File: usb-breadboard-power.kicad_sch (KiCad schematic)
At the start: 48 parts, among them J1 USB_C_Receptacle_PowerOnly_6P, J2 Conn_02x02, J3 Conn_02x02, J4 Conn_01x03, Q3 DMP6110, SW1 SW_DIP_x03, U1 CYPD3177, U2 BD33FC0FP, U3 LM339

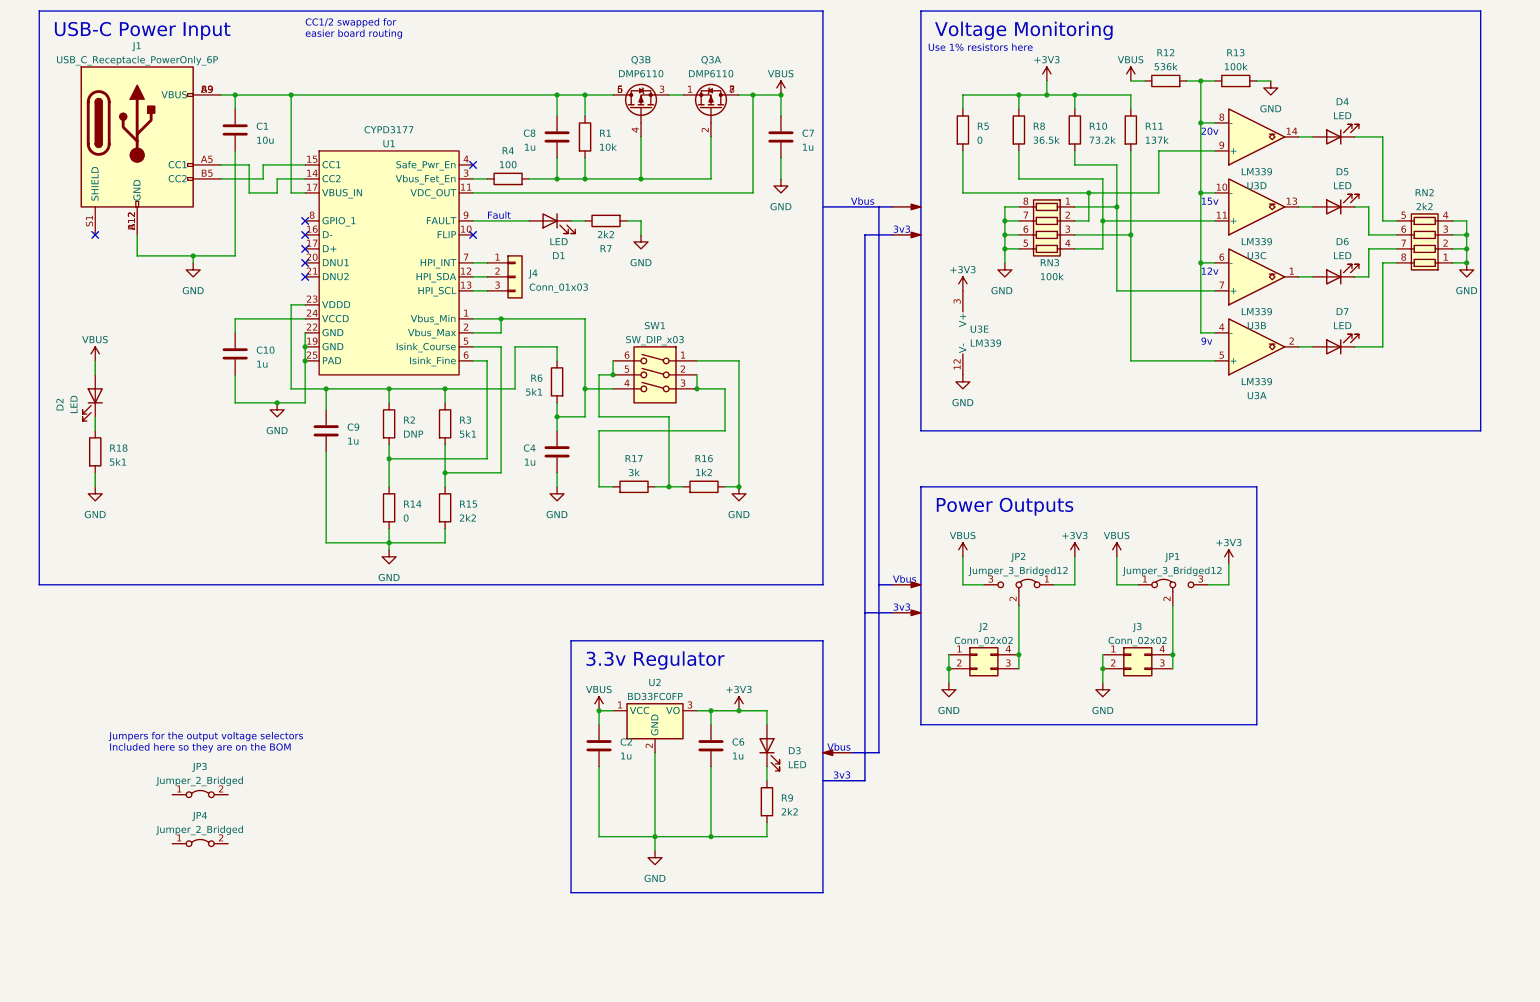
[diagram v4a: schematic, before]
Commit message: Updated gitignore and added fuse
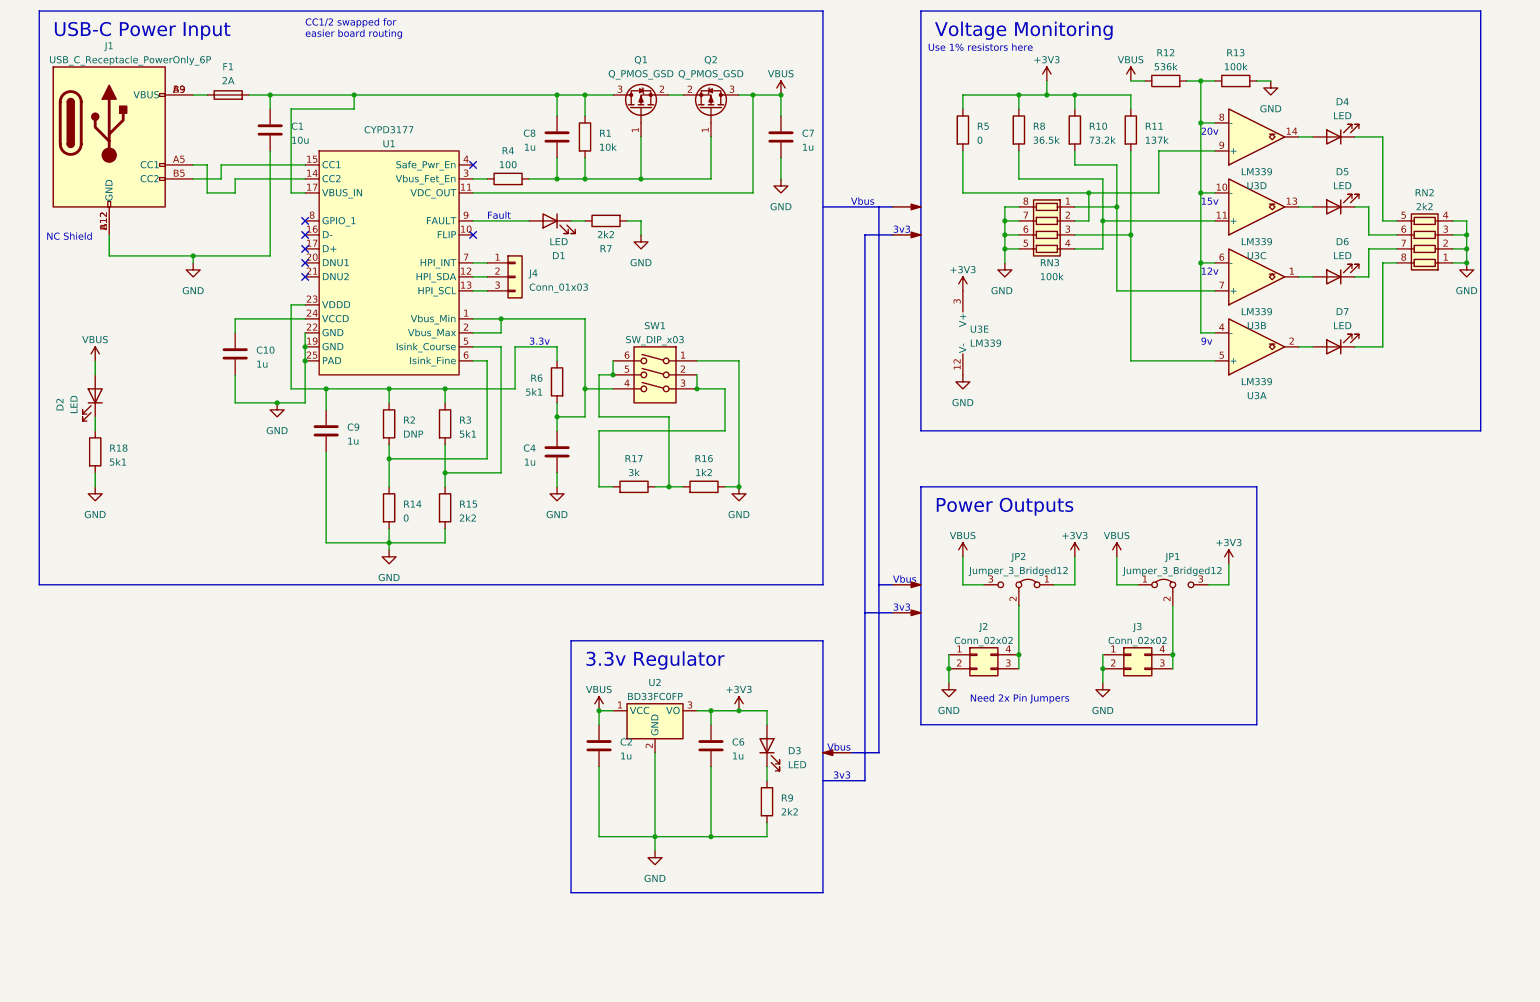
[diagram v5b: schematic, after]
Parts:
- removed JP3, JP4: Jumper_2_Bridged, symbol Jumper:Jumper_2_Bridged
- removed Q3: DMP6110, Package_SO:SO-8_5.3x6.2mm_P1.27mm, symbol Device:Q_Dual_PMOS_S1G1D2S2G2D1
- added F1: 2A, Fuse:Fuse_1812_4532Metric, symbol Device:Fuse
- added Q1, Q2: Q_PMOS_GSD, Package_TO_SOT_SMD:SOT-23-3, symbol Device:Q_PMOS_GSD
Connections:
- net VBUS: now also Q2.3 (D)
- net at U1.17 (VBUS_IN): now also C1.1, C8.1, R1.1, F1.2, Q1.3 (D)
- net at C8.2, R1.2, R4.2: now also Q1.1 (G), Q2.1 (G)
- new net: F1.1, J1.A9 (VBUS), J1.B9 (VBUS)
- new net: Q1.2 (S), Q2.2 (S)
- no-connect marks 8 -> 7
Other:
- note added: "3.3v"
- note added: "NC Shield"
- note added: "Need 2x Pin Jumpers"
- note removed: "Jumpers for the output voltage selectors Included here so they are on the BOM"
- moved on the sheet: C1

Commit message: More small fixes
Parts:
- R10: value 73.2k -> 90.9k; DPN-m 652-CR1206FX-7322ELF -> 652-CR1206FX-9092ELF; MPN-m CR1206-FX-7322ELF -> CR1206FX-9092ELF
- R11: value 137k -> 162k; DPN-m 652-CR1206FX-1373ELF -> 652-CR1206FX-1623ELF; MPN-m CR1206-FX-1373ELF -> CR1206FX-1623ELF
- R5: value 0 -> 10.5k; DPN-m 652-CR1206-J/-000ELF -> 652-CR1206FX-1052ELF; MPN-m CR1206-J/-000ELF -> CR1206FX-1052ELF
- R8: value 36.5k -> 49.9k; DPN-m 652-CR1206FX-3652ELF -> 652-CR1206FX-4992ELF; MPN-m CR1206-FX-3652ELF -> CR1206FX-4992ELF
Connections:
- net at U1.17 (VBUS_IN): now also C1.1, C8.1, F1.2, Q1.3 (D), R1.1
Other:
- note added: "3.3v internal"
- note added: "Check this is correct"
- note added: "Request 2A from the PSU"
- note removed: "3.3v"
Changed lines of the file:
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@@
     (effects (font (size 1.27 1.27)) (justify left bottom))
   )
-  (text "3.3v" (at 106.68 78.74 0)
+  (text "3.3v internal" (at 102.87 78.74 0)
     (effects (font (size 1.27 1.27)) (justify left bottom))
   )
@@
     (effects (font (size 1.27 1.27)) (justify left bottom))
   )
+  (text "Request 2A from\nthe PSU" (at 85.09 118.11 0)
+    (effects (font (size 1.27 1.27)) (justify left bottom))
+  )
   (text "Vbus" (at 165.1 53.34 0)
     (effects (font (size 1.27 1.27)) (justify left bottom))
@@
   )
   (text "Vbus" (at 172.72 121.92 0)
+    (effects (font (size 1.27 1.27)) (justify left bottom))
+  )
+  (text "Check this is correct" (at 107.95 57.15 0)
     (effects (font (size 1.27 1.27)) (justify left bottom))
   )
@@
       (effects (font (size 1.27 1.27)) (justify left))
     )
-    (property "Value" "73.2k" (at 208.28 41.275 0)
+    (property "Value" "90.9k" (at 208.28 41.275 0)
       (effects (font (size 1.27 1.27)) (justify left))
     )
@@
       (effects (font (size 1.27 1.27)) hide)
     )
-    (property "DPN-m" "652-CR1206FX-7322ELF" (at 205.74 39.37 0)
-      (effects (font (size 1.27 1.27)) hide)
-    )
-    (property "MPN-m" "CR1206-FX-7322ELF" (at 205.74 39.37 0)
+    (property "DPN-m" "652-CR1206FX-9092ELF" (at 205.74 39.37 0)
+      (effects (font (size 1.27 1.27)) hide)
+    )
+    (property "MPN-m" "CR1206FX-9092ELF" (at 205.74 39.37 0)
       (effects (font (size 1.27 1.27)) hide)
     )
@@
       (effects (font (size 1.27 1.27)) (justify left))
     )
-    (property "Value" "0" (at 187.96 41.275 0)
+    (property "Value" "10.5k" (at 187.96 41.275 0)
       (effects (font (size 1.27 1.27)) (justify left))
     )
@@
       (effects (font (size 1.27 1.27)) hide)
     )
-    (property "DPN-m" "652-CR1206-J/-000ELF " (at 185.42 39.37 0)
-      (effects (font (size 1.27 1.27)) hide)
-    )
-    (property "MPN-m" "CR1206-J/-000ELF " (at 185.42 39.37 0)
+    (property "DPN-m" "652-CR1206FX-1052ELF" (at 185.42 39.37 0)
+      (effects (font (size 1.27 1.27)) hide)
+    )
+    (property "MPN-m" "CR1206FX-1052ELF" (at 185.42 39.37 0)
       (effects (font (size 1.27 1.27)) hide)
     )
@@
       (effects (font (size 1.27 1.27)) (justify left))
     )
-    (property "Value" "137k" (at 218.44 41.275 0)
+    (property "Value" "162k" (at 218.44 41.275 0)
       (effects (font (size 1.27 1.27)) (justify left))
     )
@@
       (effects (font (size 1.27 1.27)) hide)
     )
-    (property "DPN-m" "652-CR1206FX-1373ELF" (at 215.9 39.37 0)
-      (effects (font (size 1.27 1.27)) hide)
-    )
-    (property "MPN-m" "CR1206-FX-1373ELF" (at 215.9 39.37 0)
+    (property "DPN-m" "652-CR1206FX-1623ELF" (at 215.9 39.37 0)
+      (effects (font (size 1.27 1.27)) hide)
+    )
+    (property "MPN-m" "CR1206FX-1623ELF" (at 215.9 39.37 0)
       (effects (font (size 1.27 1.27)) hide)
     )
@@
       (effects (font (size 1.27 1.27)) (justify left))
     )
-    (property "Value" "36.5k" (at 198.12 41.275 0)
+    (property "Value" "49.9k" (at 198.12 41.275 0)
       (effects (font (size 1.27 1.27)) (justify left))
     )
@@
       (effects (font (size 1.27 1.27)) hide)
     )
-    (property "DPN-m" "652-CR1206FX-3652ELF" (at 195.58 39.37 0)
-      (effects (font (size 1.27 1.27)) hide)
-    )
-    (property "MPN-m" "CR1206-FX-3652ELF" (at 195.58 39.37 0)
-      (effects (font (size 1.27 1.27)) hide)
-    )
+    (property "DPN-m" "652-CR1206FX-4992ELF" (at 195.58 39.37 0)
+      (effects (font (size 1.27 1.27)) hide)
+    )
+    (property "MPN-m" "CR1206FX-4992ELF" (at 195.58 39.37 0)
+      (effects (font (size 1.27 1.27)) hide)
+    )

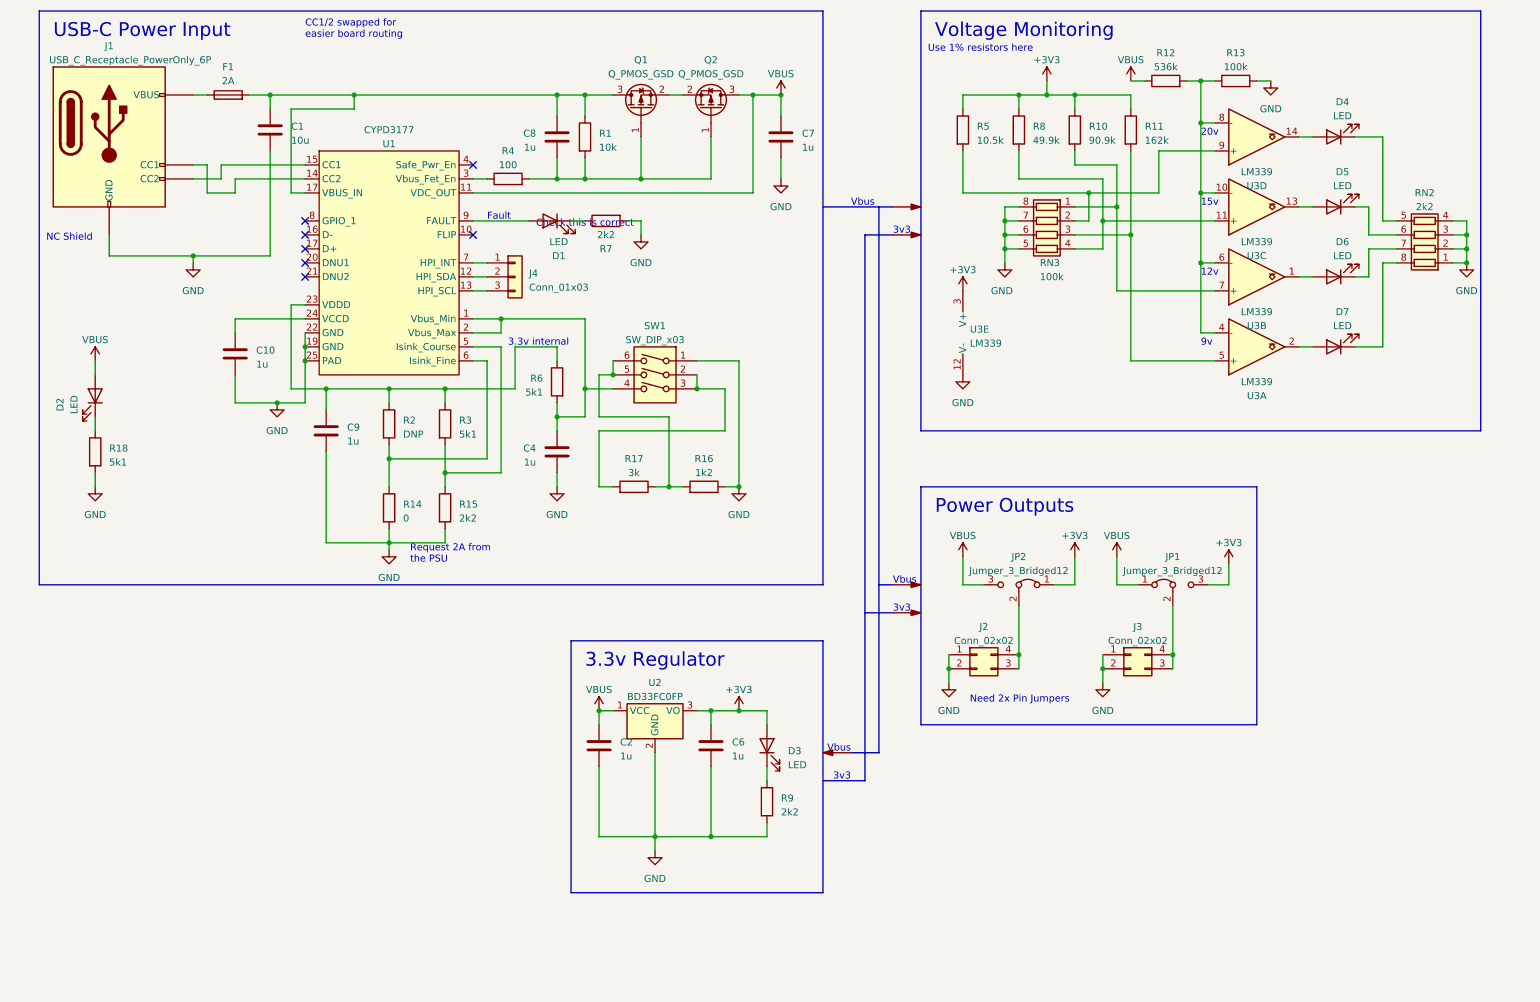
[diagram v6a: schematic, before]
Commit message: Fixed switching reg layout
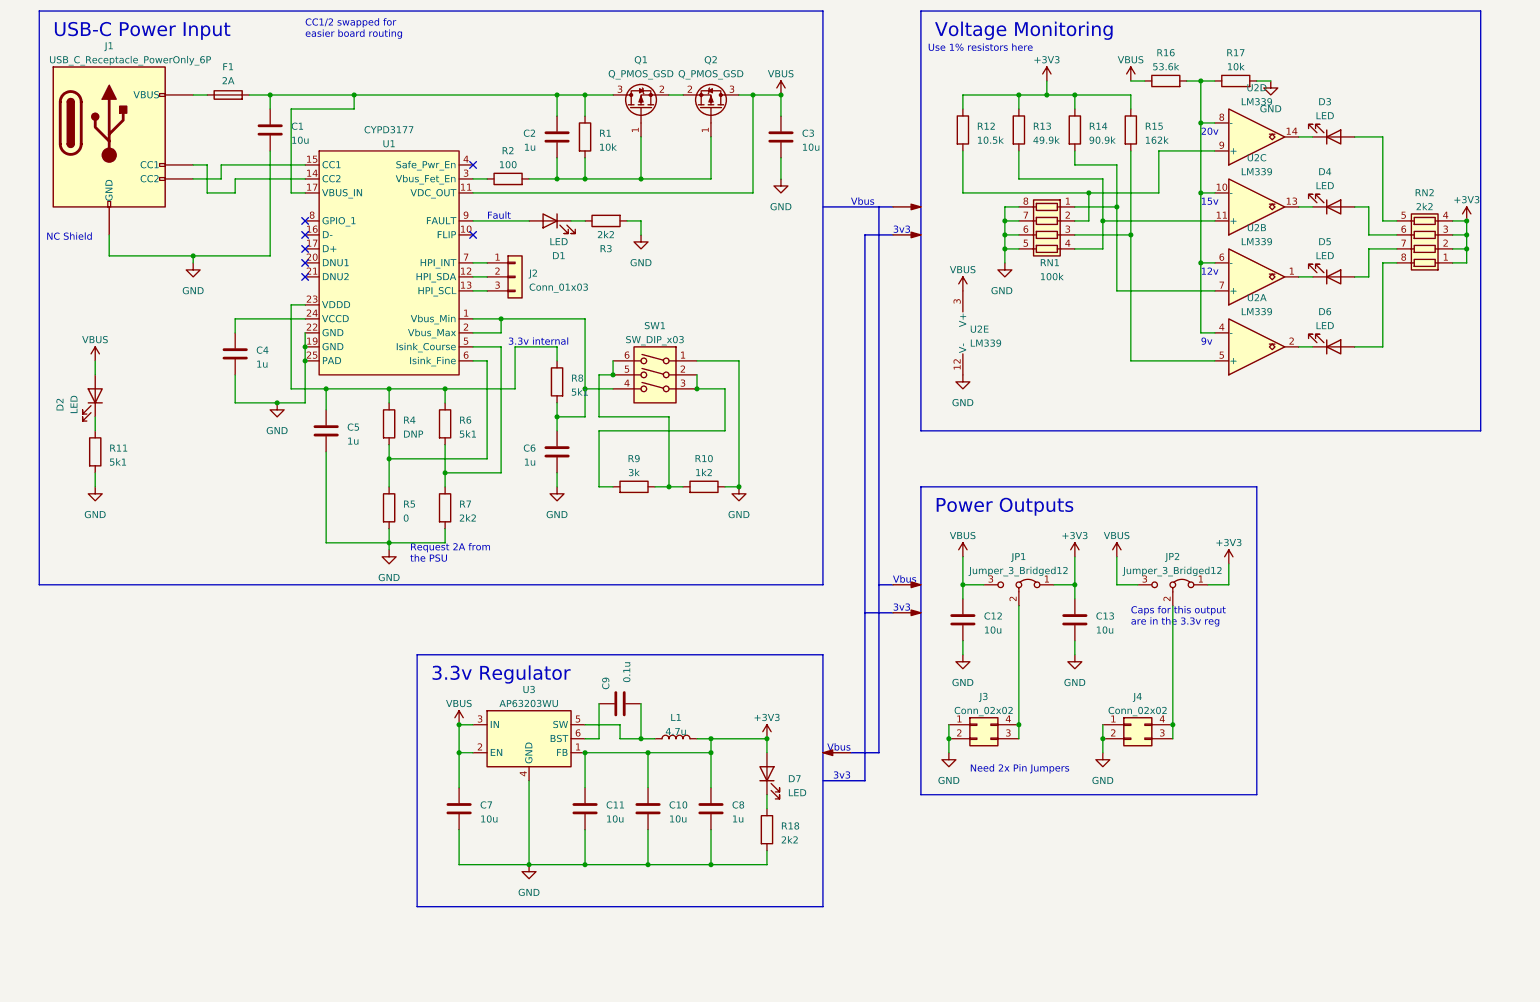
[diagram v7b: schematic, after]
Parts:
- removed U2: BD33FC0FP, Package_TO_SOT_SMD:TO-252-2, symbol Regulator_Linear:BD33FC0FP
- added C10, C11, C12, C13: 10u, Capacitor_SMD:C_1206_3216Metric, symbol Device:C
- added C9: 0.1u, Capacitor_SMD:C_1206_3216Metric, symbol Device:C
- added L1: 4.7u, Inductor_SMD:L_1210_3225Metric, symbol Device:L
- added U3: AP63203WU, Package_TO_SOT_SMD:TSOT-23-6, symbol Regulator_Switching:AP63205WU
- C1: DPN-m 187-CL31A106KAHNNNE -> 187-CL31A106MBHNNNE; MPN-m CL31A106KAHNNNE -> CL31A106MBHNNNE
- C2: renamed from C8; DPN-m 187-CL31B105KAHNNNE -> 187-CL31B105KBHNFNE; MPN-m CL31B105KAHNNNE -> CL31B105KBHNFNE
- C3: renamed from C7; value 1u -> 10u; DPN-m 187-CL31B105KAHNNNE -> 187-CL31A106MBHNNNE; MPN-m CL31B105KAHNNNE -> CL31A106MBHNNNE
- C4: renamed from C10; DPN-m 187-CL31B105KAHNNNE -> 187-CL31B105KBHNFNE; MPN-m CL31B105KAHNNNE -> CL31B105KBHNFNE
- C5: renamed from C9; DPN-m 187-CL31B105KAHNNNE -> 187-CL31B105KBHNFNE; MPN-m CL31B105KAHNNNE -> CL31B105KBHNFNE
- C6: renamed from C4; DPN-m 187-CL31B105KAHNNNE -> 187-CL31B105KBHNFNE; MPN-m CL31B105KAHNNNE -> CL31B105KBHNFNE
- C7: renamed from C2; value 1u -> 10u; DPN-m 187-CL31B105KAHNNNE -> 187-CL31A106MBHNNNE; MPN-m CL31B105KAHNNNE -> CL31A106MBHNNNE
- C8: renamed from C6; DPN-m 187-CL31B105KAHNNNE -> 187-CL31B105KBHNFNE; MPN-m CL31B105KAHNNNE -> CL31B105KBHNFNE
- R16: renamed from R12; value 536k -> 53.6k; DPN-m 652-CR1206FX-5363ELF -> 652-CR1206FX-5362ELF; MPN-m CR1206-FX-5363ELF -> CR1206-FX-5362ELF
- R17: renamed from R13; value 100k -> 10k; DPN-m 652-CR1206FX-1003ELF -> 652-CR1206FX-1002ELF; MPN-m CR1206-FX-1003ELF -> CR1206-FX-1002ELF
- renumbered D4 to D3, D5 to D4, D6 to D5, D7 to D6, D3 to D7, J4 to J2, J2 to J3, J3 to J4, JP2 to JP1, JP1 to JP2, R16 to R10, R18 to R11, R5 to R12, R8 to R13, R10 to R14, R11 to R15, R9 to R18, R4 to R2, R7 to R3, R2 to R4, R14 to R5, R3 to R6, R15 to R7, R6 to R8, R17 to R9, RN3 to RN1, U3 to U2
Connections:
- net +3V3: now also JP2.1 (A), RN2.1 (R1.1), RN2.2 (R2.1), RN2.3 (R3.1), RN2.4 (R4.1), C10.1, C11.1, C13.1, L1.2, U3.1 (FB); no longer JP2.3 (B), U2.3 (V+)
- net GND: now also C10.2, C11.2, C12.2, C13.2, U3.4 (GND); no longer RN2.1 (R1.1), RN2.2 (R2.1), RN2.3 (R3.1), RN2.4 (R4.1)
- net VBUS: now also JP2.3 (B), U2.3 (V+), C12.1, U3.2 (EN), U3.3 (IN); no longer JP2.1 (A)
- net at U2.14: now also D3.1 (K); no longer D3.2 (A)
- net at U2.2: now also D6.1 (K); no longer D6.2 (A)
- net at D4.1 (K): now also U2.13; no longer RN2.6 (R3.2)
- net at D4.2 (A): now also RN2.6 (R3.2); no longer U2.13
- net at U1.17 (VBUS_IN): now also C1.1, C2.1, F1.2, Q1.3 (D), R1.1
- net at RN2.5 (R4.2): now also D3.2 (A); no longer D3.1 (K)
- net at U2.1: now also D5.1 (K); no longer D5.2 (A)
- net at RN2.7 (R2.2): now also D5.2 (A); no longer D5.1 (K)
- net at RN2.8 (R1.2): now also D6.2 (A); no longer D6.1 (K)
- new net: C9.1, L1.1, U3.5 (SW)
- new net: C9.2, U3.6 (BST)
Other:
- note added: "Caps for this output are in the 3.3v reg"
- note removed: "Check this is correct"
- moved on the sheet: C7, C8, D3, D4, D5, D6, D7, J3, J4, R18

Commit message: Confirmed BOM
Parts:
- C9: DPN-m 187-CL31B104KBCNNNC -> 187-CL31B104KBCNNND; MPN-m CL31B104KBCNNNC -> CL31B104KBCNNND
- JP1, JP2: now left out of the parts list
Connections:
- net at U1.17 (VBUS_IN): now also C1.1, C2.1, F1.2, Q1.3 (D), R1.1
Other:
- note added: "All resistors 1206 1/4W 1% All caps 1206 50V"
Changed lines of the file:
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@@
     (effects (font (size 1.27 1.27)) (justify right bottom))
+  )
+  (text "All resistors 1206 1/4W 1%\nAll caps 1206 50V" (at 255.27 186.69 0)
+    (effects (font (size 1.27 1.27)) (justify left bottom))
   )
   (text "Fault" (at 99.06 55.88 0)
@@
   )
   (symbol (lib_id "Jumper:Jumper_3_Bridged12") (at 195.58 121.92 0) (mirror y) (unit 1)
-    (in_bom yes) (on_board yes) (dnp no)
+    (in_bom no) (on_board yes) (dnp no)
     (property "Reference" "JP1" (at 195.58 116.84 0)
       (effects (font (size 1.27 1.27)))
@@
       (effects (font (size 1.27 1.27)) hide)
     )
-    (property "DPN-m" "187-CL31B104KBCNNNC" (at 123.19 143.51 0)
-      (effects (font (size 1.27 1.27)) hide)
-    )
-    (property "MPN-m" "CL31B104KBCNNNC" (at 123.19 143.51 0)
+    (property "DPN-m" "187-CL31B104KBCNNND" (at 123.19 143.51 0)
+      (effects (font (size 1.27 1.27)) hide)
+    )
+    (property "MPN-m" "CL31B104KBCNNND" (at 123.19 143.51 0)
       (effects (font (size 1.27 1.27)) hide)
     )
@@
   )
   (symbol (lib_id "Jumper:Jumper_3_Bridged12") (at 223.52 121.92 0) (mirror y) (unit 1)
-    (in_bom yes) (on_board yes) (dnp no)
+    (in_bom no) (on_board yes) (dnp no)
     (property "Reference" "JP2" (at 223.52 116.84 0)
       (effects (font (size 1.27 1.27)))
